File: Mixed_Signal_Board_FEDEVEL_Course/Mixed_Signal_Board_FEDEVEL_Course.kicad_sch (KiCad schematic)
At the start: 0 parts

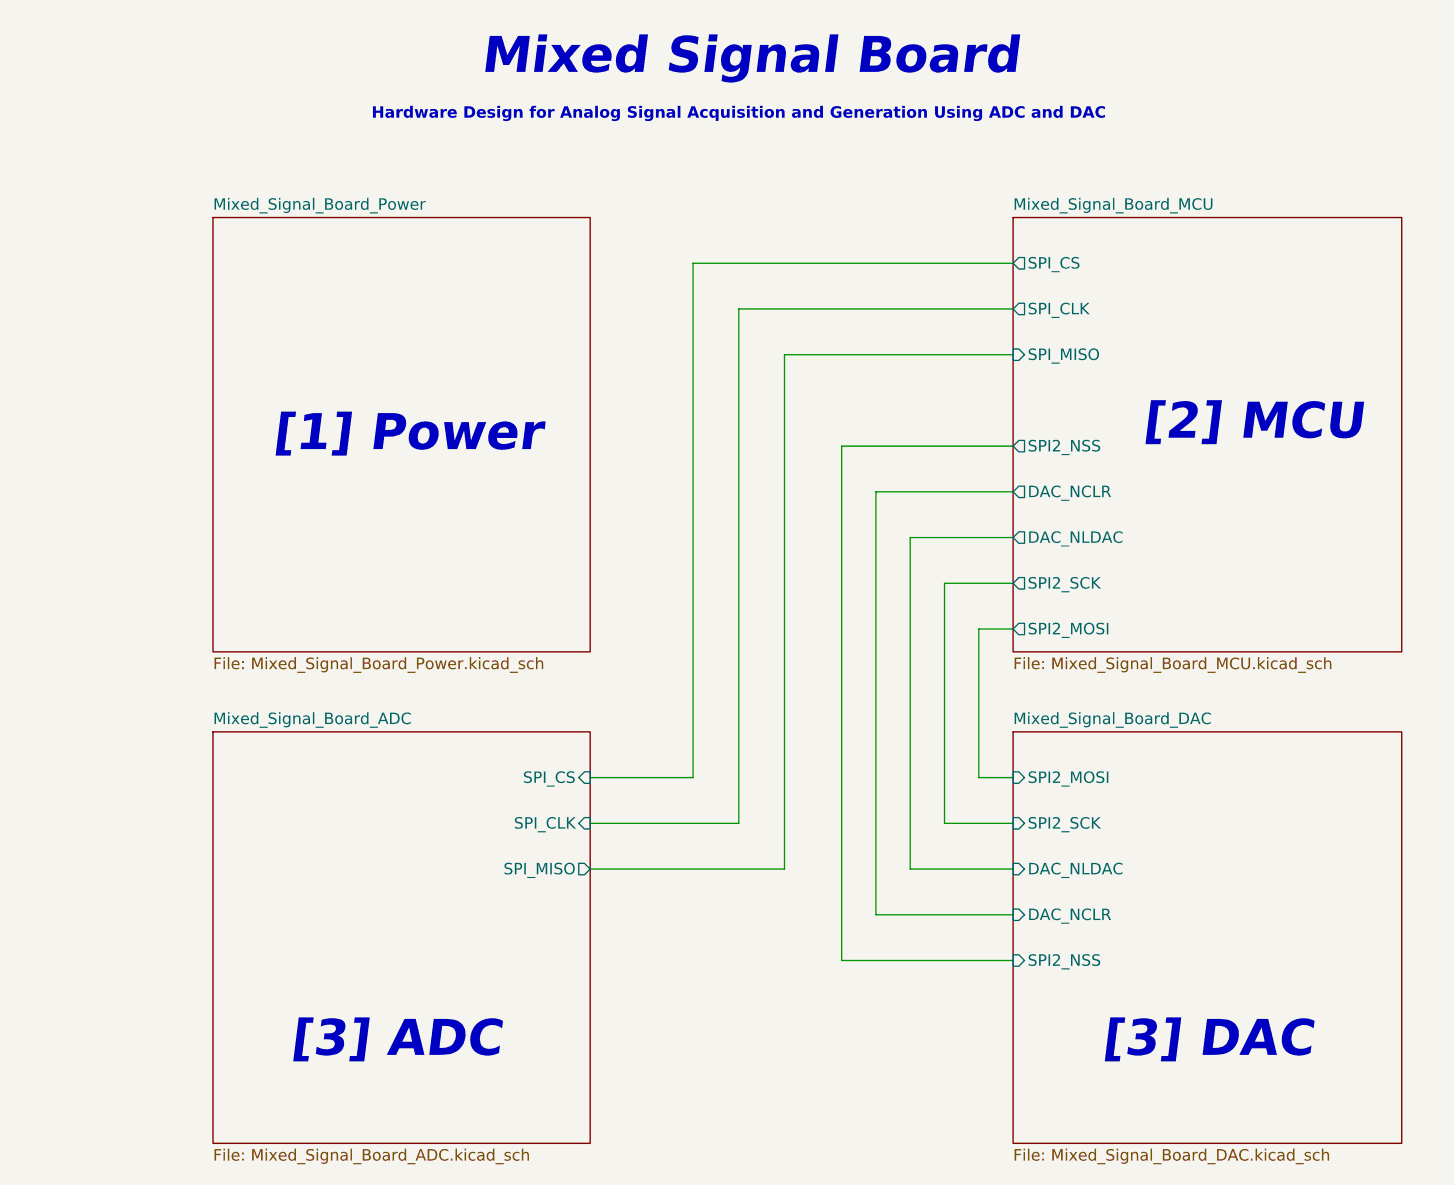
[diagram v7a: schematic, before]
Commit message: Solve the errors of sch after running the DRC
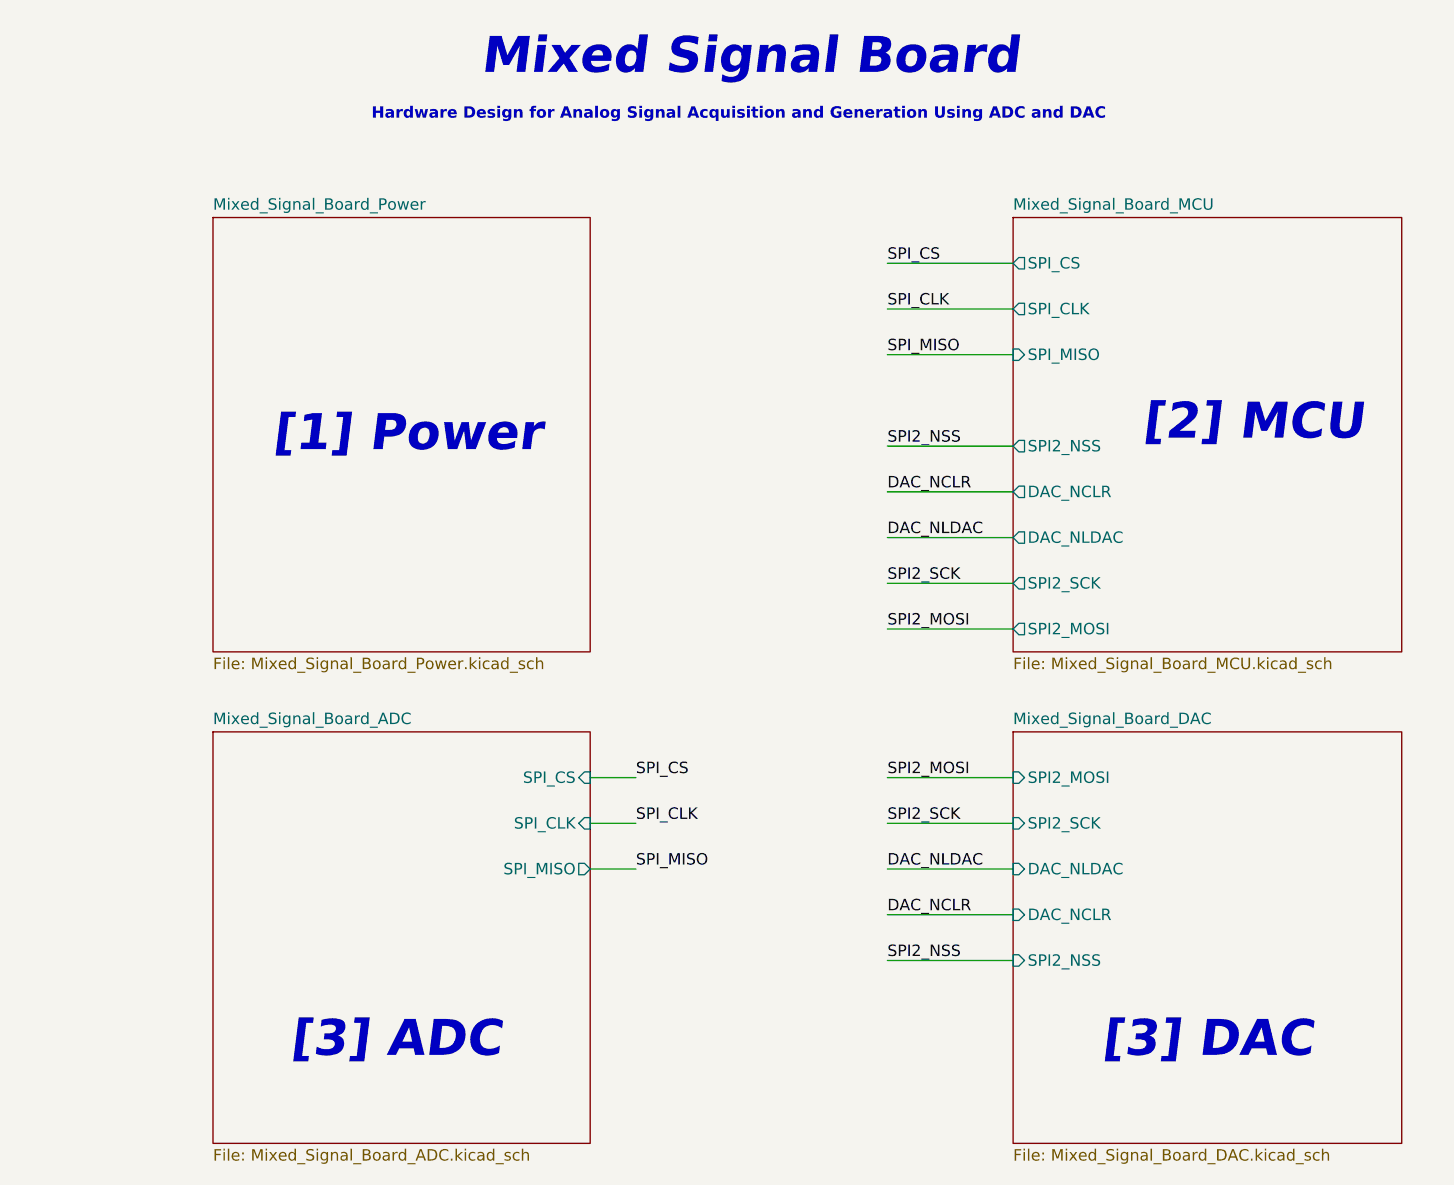
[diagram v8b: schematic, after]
